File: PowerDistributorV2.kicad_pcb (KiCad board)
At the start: 2 copper layers, 100 x 29 mm, 22 parts, among them J1 F1, J10 + D2 -, J11 + D3 -, J12 + D4 -, J13 + D5 -, J14 + D6 -, J15 + D7 -, J16 + D8 -, J17 + PWR -, J2 F2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

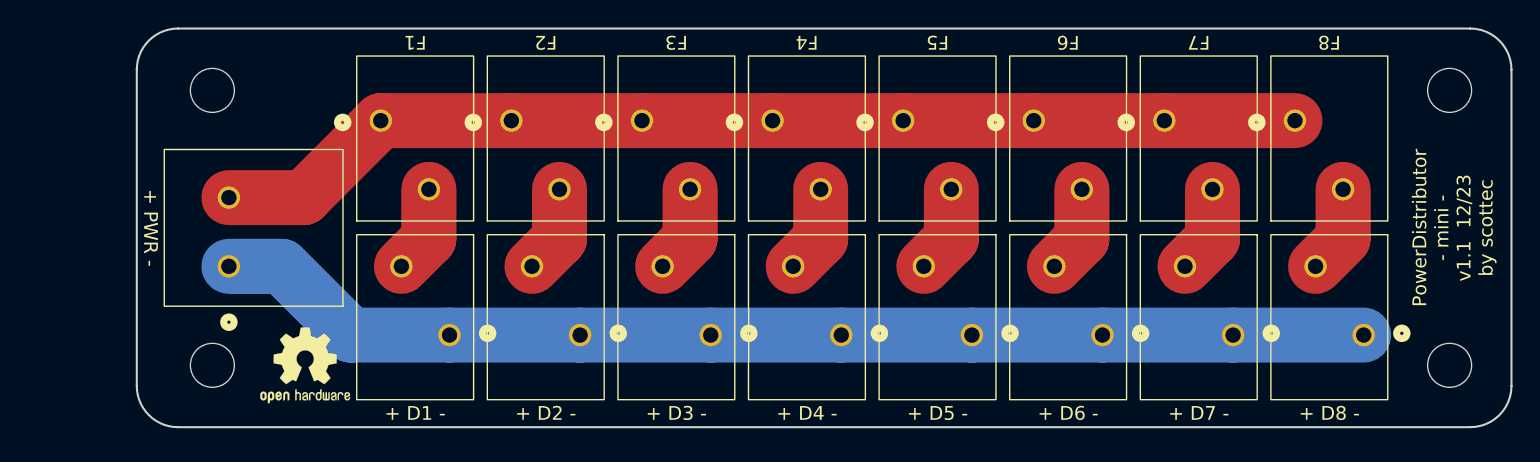
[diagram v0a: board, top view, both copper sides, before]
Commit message: change power connector, add markings, logos and measurements
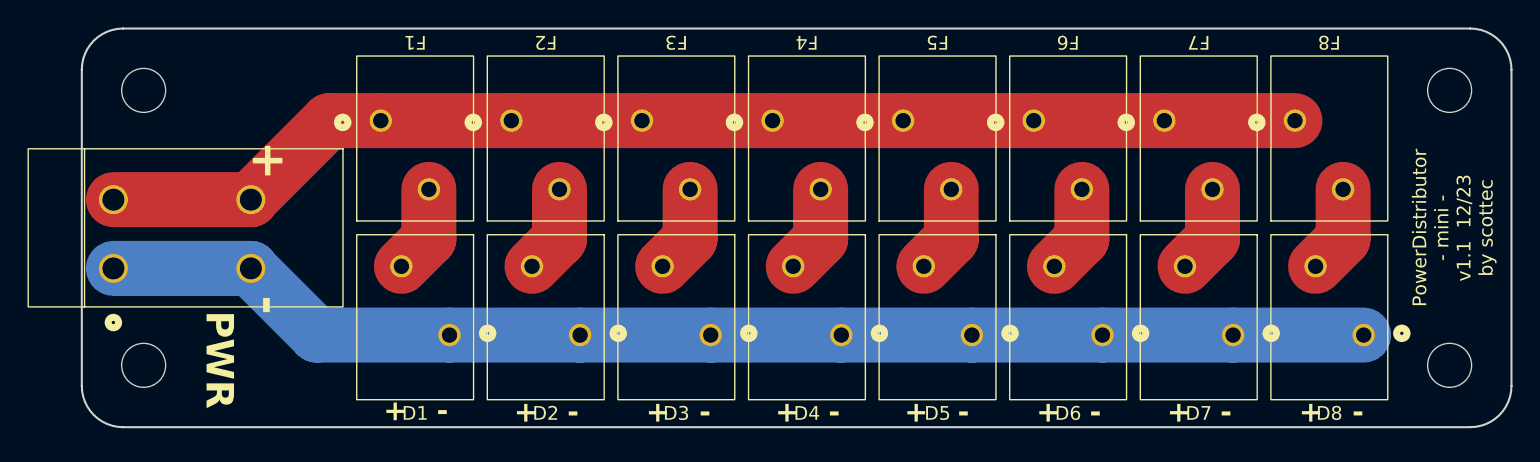
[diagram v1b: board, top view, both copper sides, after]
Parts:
- added REF**: KiCad-Logo_5mm_SilkScreen, Symbol:KiCad-Logo_5mm_SilkScreen, B.Cu at (98.4, 105.1)
- J10: value + D2 - -> D2
- J11: value + D3 - -> D3
- J12: value + D4 - -> D4
- J13: value + D5 - -> D5
- J14: value + D6 - -> D6
- J15: value + D7 - -> D7
- J16: value + D8 - -> D8
- J17: value + PWR - -> PWR; footprint GSI_footprints:Wago-250-502 -> GSI_footprints:Wago-745-102
- J9: value + D1 - -> D1
- REF**: moved to B.Cu
- moved REF** 72.5 mm to (172.1, 104.9), turned to 180 degrees
- moved J17 8.40 mm to (85.6, 97.9)
- moved H1 5.00 mm to (87.8, 84.9)
- moved H3 5.00 mm to (87.8, 104.9)
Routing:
- net VDC: track 79.9 -> 88.4 mm
- net GND: track 84.6 -> 93.0 mm
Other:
- board size 100 x 29 mm -> 104 x 29 mm
- board text added: "+ -"
- board text added: "Keine Macht dem Kabelchaos!"
- board text added: "M3"
